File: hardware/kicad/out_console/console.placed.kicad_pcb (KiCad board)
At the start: 2 copper layers, 115 x 95 mm, 54 parts, among them J1 RaspberryPi_Pico_Common_THT, J10 JST_XH_B2B-XH-A_1x02_P2.50mm_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, J11 JST_XH_B2B-XH-A_1x02_P2.50mm_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, J12 JST_XH_B2B-XH-A_1x02_P2.50mm_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, J13 JST_XH_B2B-XH-A_1x02_P2.50mm_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, J14 JST_XH_B2B-XH-A_1x02_P2.50mm_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, J15 JST_XH_B2B-XH-A_1x02_P2.50mm_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, J16 JST_XH_B2B-XH-A_1x02_P2.50mm_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, J17 JST_XH_B2B-XH-A_1x02_P2.50mm_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, J18 JST_XH_B2B-XH-A_1x02_P2.50mm_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, J19 JST_XH_B2B-XH-A_1x02_P2.50mm_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, J2 IDC-Header_2x20_P2.54mm_Verti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, J20 JST_XH_B3B-XH-A_1x03_P2.50mm_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, J21 JST_XH_B3B-XH-A_1x03_P2.50mm_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, J22 PinHeader_2x04_P2.54mm_Vertic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, J3 JST_XH_B4B-XH-A_1x04_P2.50mm_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, J4 JST_XH_B3B-XH-A_1x03_P2.50mm_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, J5 JST_XH_B2B-XH-A_1x02_P2.50mm_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, J6 JST_XH_B8B-XH-A_1x08_P2.50mm_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, J7 JST_XH_B3B-XH-A_1x03_P2.50mm_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, J8 JST_XH_B2B-XH-A_1x02_P2.50mm_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, J9 JST_XH_B3B-XH-A_1x03_P2.50mm_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, U1 DIP-14_W7.62mm, U2 DIP-6_W7.62mm

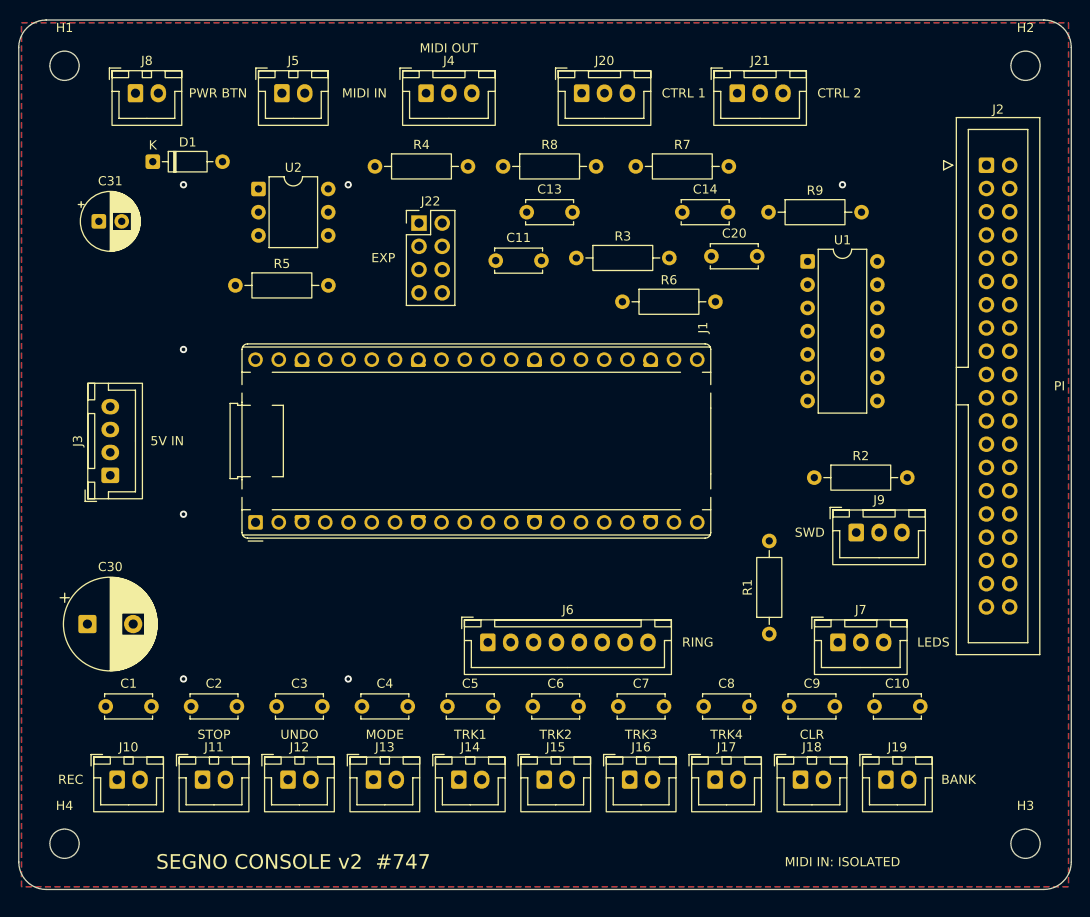
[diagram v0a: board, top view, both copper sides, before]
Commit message: style(hardware): put the console board's connectors and labels on shared lines
Purely cosmetic; no net or gate changes. The board read as scattered because
three separate things were each individually legal and collectively arbitrary:

- The rear-panel headers sat at 14/30/47/64/81 -- three different gaps, and the
  group off-centre. They are now on an even 17.5 mm pitch centred on x 54, the
  same centre line the switch row already used, and the resistors below them sit
  on those same centres rather than a 15 mm pitch of their own. Two pitches
  beating against each other is what made the band look crooked.
- Labels were placed by a nearest-free-gap search, so the rear-panel row came out
  "above, right, above, right, right" and REC sat left of its header while its
  nine neighbours sat above. The two rows that matter are now pinned to one y;
  the search remains as fallback for one-off headers.
- R1 was the only vertical resistor among twelve horizontals, which reads as an
  accident rather than a decision.

Still 0 DRC violations, 0 unconnected.

Refs #747
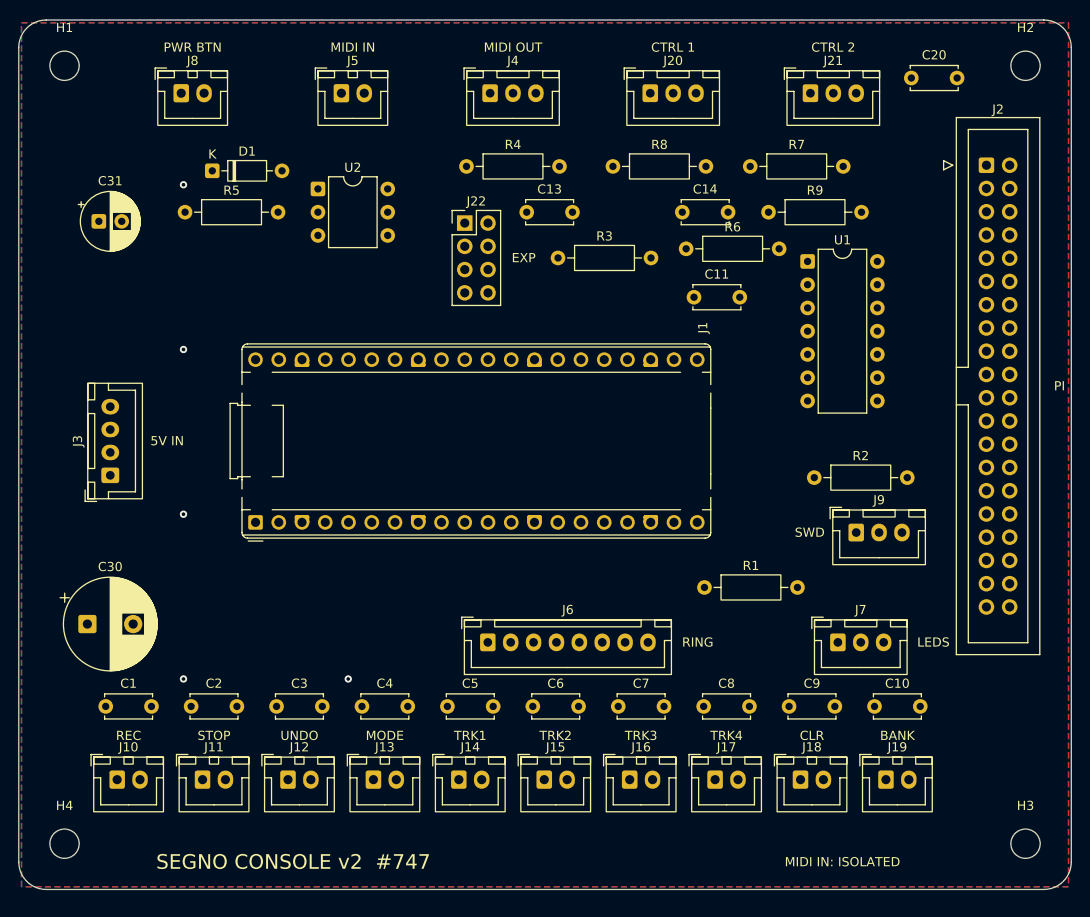
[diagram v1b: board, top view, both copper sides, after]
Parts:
- moved C20 29.3 mm to (197.5, 66.3)
- moved C11 22.0 mm to (173.8, 90.3)
- moved R7 12.5 mm to (179.9, 76.0)
- moved R8 12.0 mm to (164.9, 76.0)
- moved R4 10.0 mm to (148.9, 76.0)
- moved R5 9.71 mm to (118.2, 81.0)
- moved R6 9.05 mm to (172.9, 85.0)
- moved R1 8.71 mm to (174.9, 122.0), turned to 0 degrees
- moved J21 8.00 mm to (186.5, 68.0)
- moved J20 7.50 mm to (169.0, 68.0)
- moved J4 7.00 mm to (151.5, 68.0)
- moved D1 6.58 mm to (121.1, 76.5)
- moved J5 6.50 mm to (135.2, 68.0)
- moved U2 6.50 mm to (132.7, 78.5)
- moved J22 5.00 mm to (148.7, 82.2)
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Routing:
- net GND: vias 66 -> 64

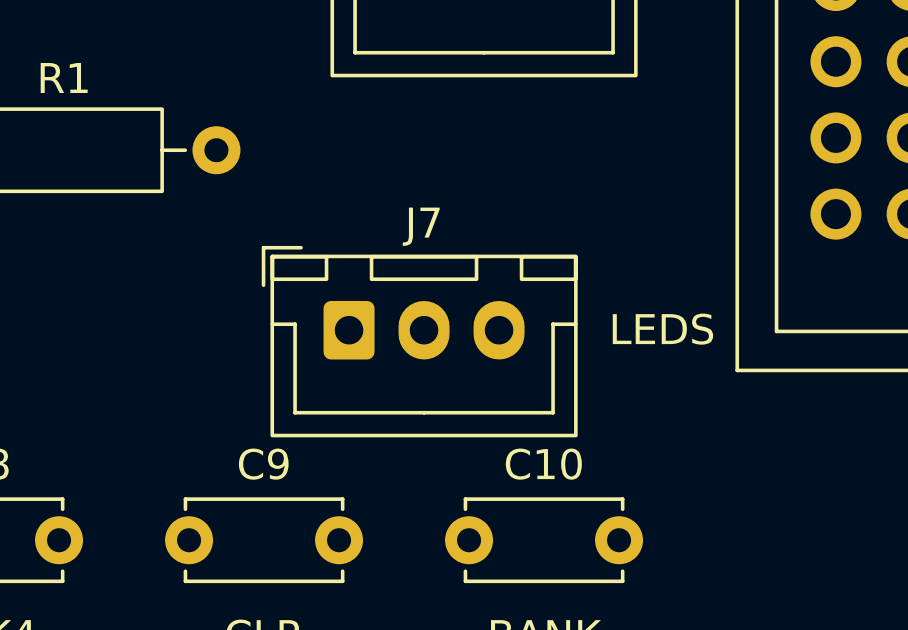
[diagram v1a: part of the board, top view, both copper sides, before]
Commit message: style(hardware): align J7 with J9 on the console board
Same 3-pin footprint, one directly below the other, sitting 2 mm apart in x --
which reads as a slip rather than a decision. No net changes; still 0 DRC
violations, 0 unconnected.

Refs #747
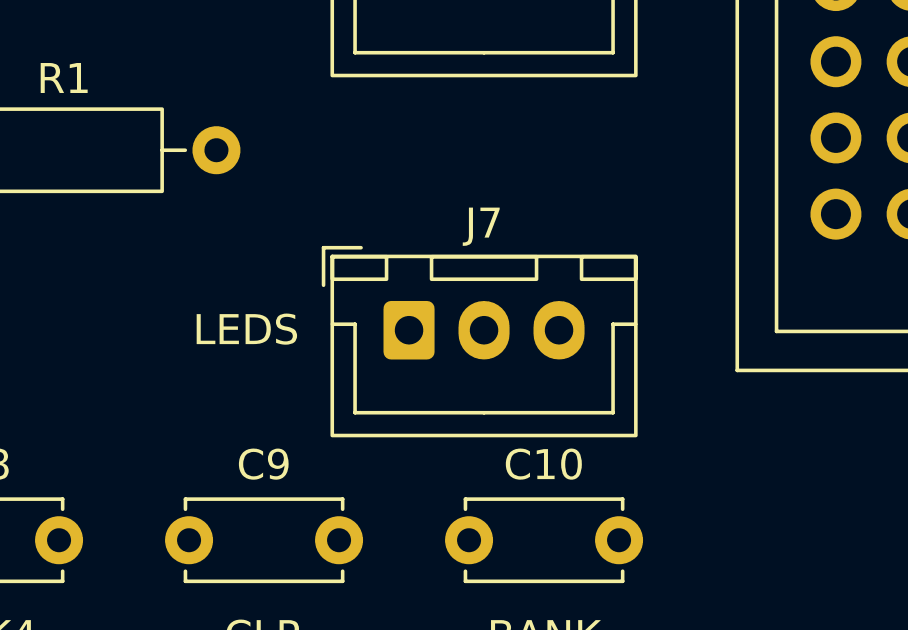
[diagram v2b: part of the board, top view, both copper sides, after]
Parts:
- moved J7 2.00 mm to (191.5, 128.0)

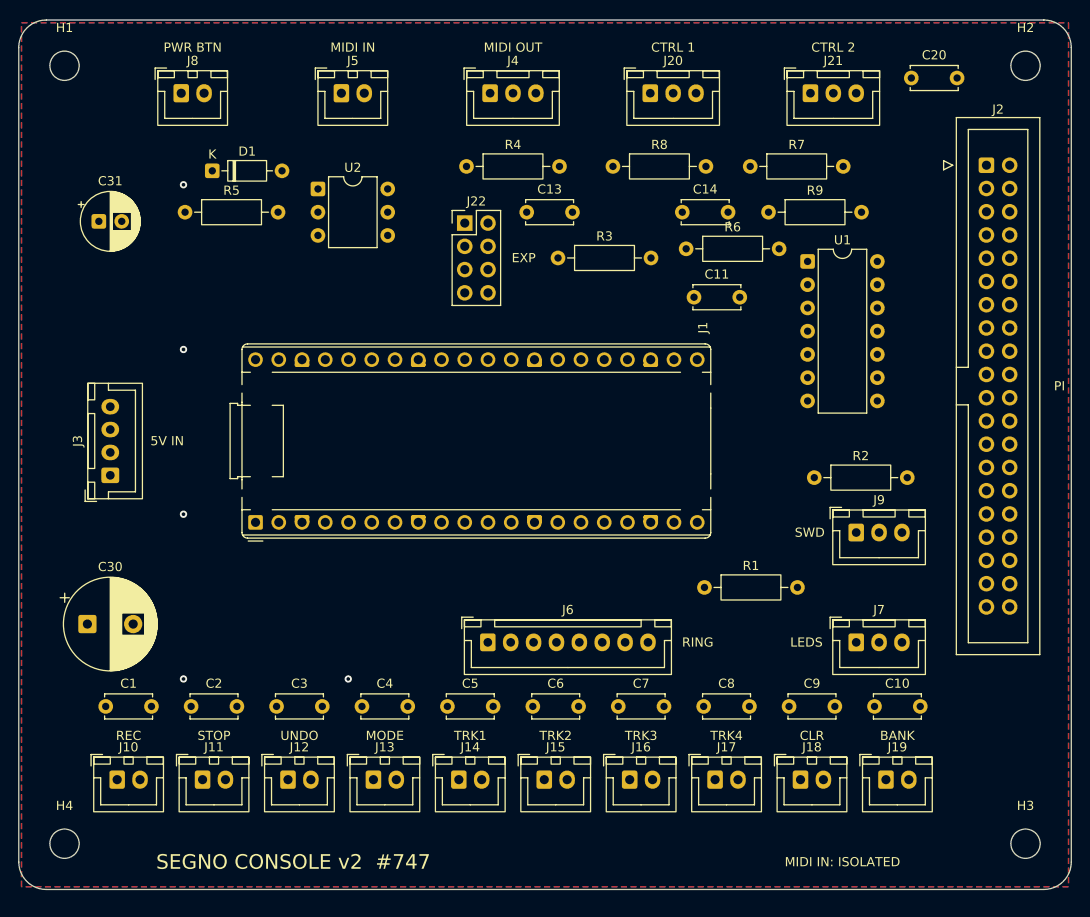
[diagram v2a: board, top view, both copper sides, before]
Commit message: feat(hardware): solder SWD to the Pico's own debug pads and centre the rows
The board would not route: RING_DATA had to climb from the module's row A to
U1's input through the corridor that the link, IND, EXP and CTRL nets all cross,
and J9 -- a 3-pin header breaking SWD out to flying wires -- sat in it. Centring
the pedal row made that corridor tighter still, so the two problems were one.

Both go away by dropping J9. Module:RaspberryPi_Pico_SMD_HandSolder carries the
three debug pads (D1/D2/D3) that the THT footprint does not, so SWCLK/GND/SWDIO
land straight on the module. The connector, its wires and the space it occupied
are gone. Conn_01x40 has no D pins, so they are added to the part explicitly --
otherwise SWD silently has nothing to attach to.

Trade: the module is soldered by its castellations, not socketed on headers, so
swapping one needs hot air. For a sealed console reflashed over SWD, correct.

Also: both connector rows now sit on the board's true centre (x 57.5) at an even
17.5 mm pitch -- the pedal row was 7.75 mm from the left edge and 14.75 from the
right -- and freerouting runs with -dct 0, cutting its 20 s idle timeout.

115x96 mm. 0 DRC violations, 0 unconnected, and it routes clean first attempt
rather than one roll in three.

Refs #747
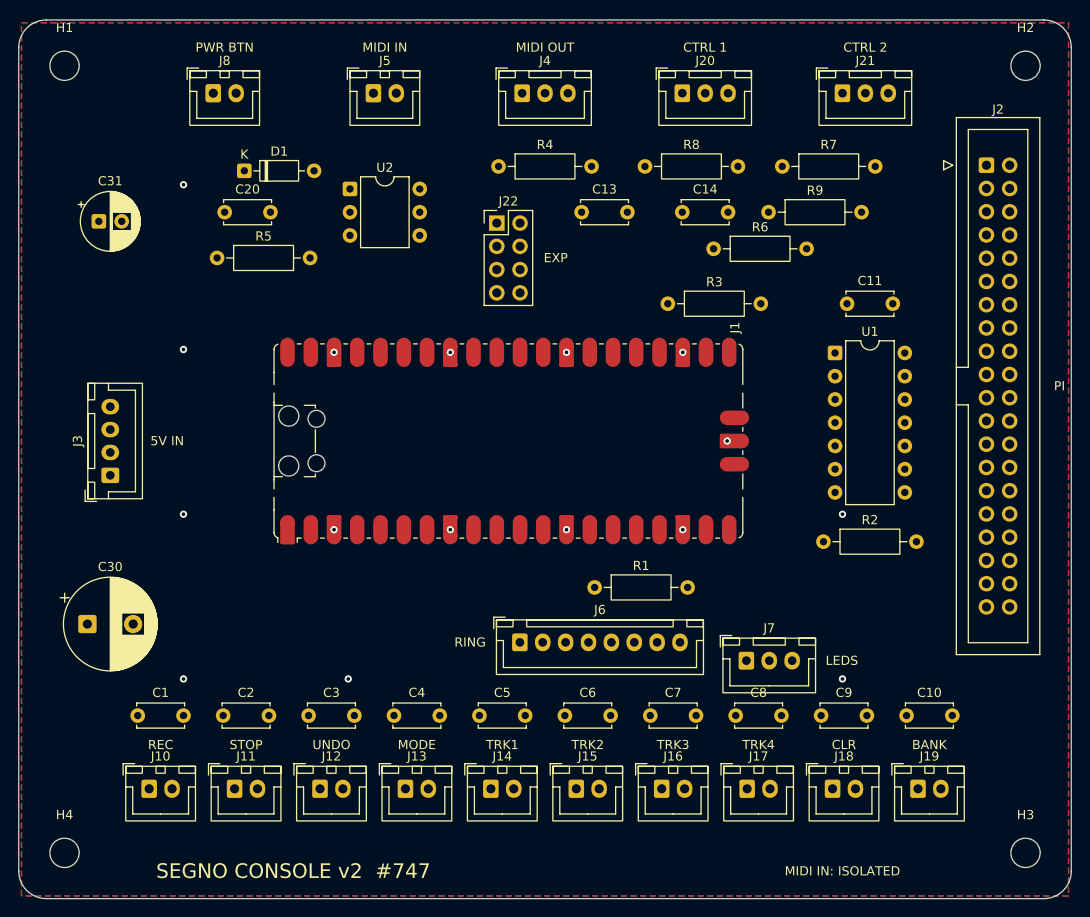
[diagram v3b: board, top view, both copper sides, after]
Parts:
- removed J9: JST_XH_B3B-XH-A_1x03_P2.50mm_Vertical, JST_XH_B3B-XH-A_1x03_P2.50mm_Vertical
- J1: value RaspberryPi_Pico_Common_THT -> RaspberryPi_Pico_SMD_HandSolder; footprint RaspberryPi_Pico_Common_THT -> RaspberryPi_Pico_SMD_HandSolder
- moved C20 76.4 mm to (122.5, 81.0)
- moved J1 29.0 mm to (153.5, 106.0)
- moved C11 16.7 mm to (190.5, 91.0)
- moved R3 13.0 mm to (170.9, 91.0)
- moved J7 12.2 mm to (179.5, 130.0)
- moved R1 12.0 mm to (162.9, 122.0)
- moved U1 10.4 mm to (189.2, 96.4)
- moved R2 7.07 mm to (187.9, 117.0)
- moved R5 6.10 mm to (121.7, 86.0)
- moved C13 6.00 mm to (161.5, 81.0)
- moved C1 3.64 mm to (113.0, 136.0)
- moved C10 3.64 mm to (197.0, 136.0)
- moved C2 3.64 mm to (122.3, 136.0)
- moved C3 3.64 mm to (131.7, 136.0)
- moved C4 3.64 mm to (141.0, 136.0)
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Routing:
- net GND: vias 64 -> 66
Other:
- board size 115 x 95 mm -> 115 x 96 mm
- board text removed: "SWD"

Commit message: fix(hardware): give the ground pours thermal relief now the Pico is SMD
The pours tied pads with solid copper. That was justified in a comment reading
"THT parts here are hand-soldered, so the usual thermal-relief argument
(wave/reflow) is moot" -- true when written, and false from the commit that made
the Pico a surface-mount module. Its nine GND pads sat in a plane on their own
layer with solid ties, which wicks the iron's heat into the plane and cold-joints
the one part that is painful to rework.

Solid was originally chosen to escape five "starved_thermal" errors from spokes
too narrow to form. That was a symptom of leaving the widths at their defaults,
not a reason to abandon relief: set explicitly (0.3 mm gap, 0.4 mm spokes) there
are none.

Two consequences, both real rather than cosmetic:
- Relief stops pads bridging the pour, which orphaned an F.Cu region. Stitch
  pitch drops 18 -> 12 mm (66 -> 83 vias). Relief and stitch pitch are one
  decision, not two.
- A 3 mm2 minimum island area drops slivers that reach a single pad and go
  nowhere; they cannot carry a return and they fail DRC as starved thermals.

Gated: any pour that ties pads solid while the board carries SMD pads now fails.
Nothing caught this transition, which is why it survived a footprint change.

0 DRC violations, 0 unconnected.

Refs #747
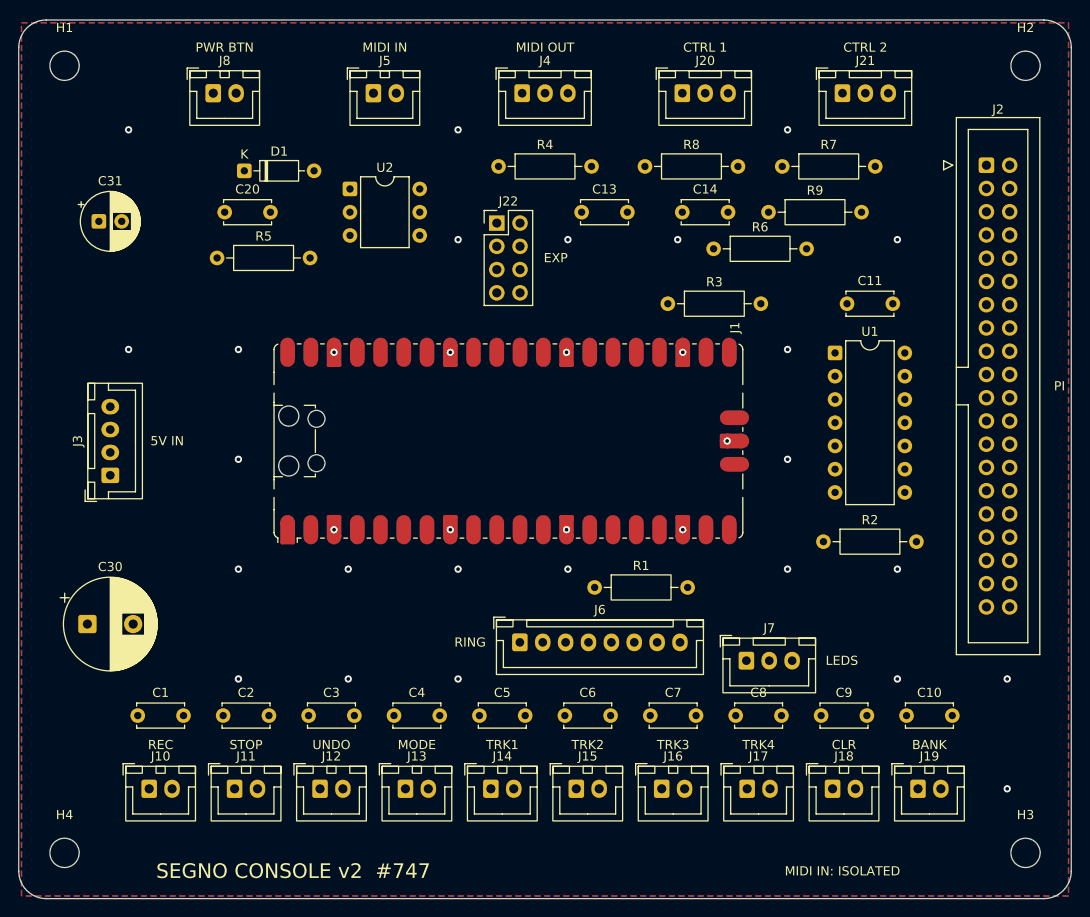
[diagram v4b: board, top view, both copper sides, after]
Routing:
- net GND: vias 66 -> 83

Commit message: fix(hardware): keep the module's USB corridor clear, and align J6 with J7
The 5 V inlet sat directly in front of the Pico's USB socket. The argument for
pointing that end into the bulk caps was that USB is not NEEDED -- VSYS is fed
from J3 and the Pi flashes over SWD -- but "not needed" quietly became "made
impossible", which is a different claim and not one anyone agreed to. J3 moves
down the left edge and C30 moves up, leaving y 40..52 clear from the socket to
the board edge.

Gated, with a negative control that reproduces exactly the shipped mistake:
anything intruding on the corridor off the module's USB end now fails.

Also J6 (RING) and J7 (LEDS) sat at y 68 and 70 -- same footprint family, side by
side, two millimetres apart for no reason. Both on 69.

0 DRC violations, 0 unconnected.

Refs #747
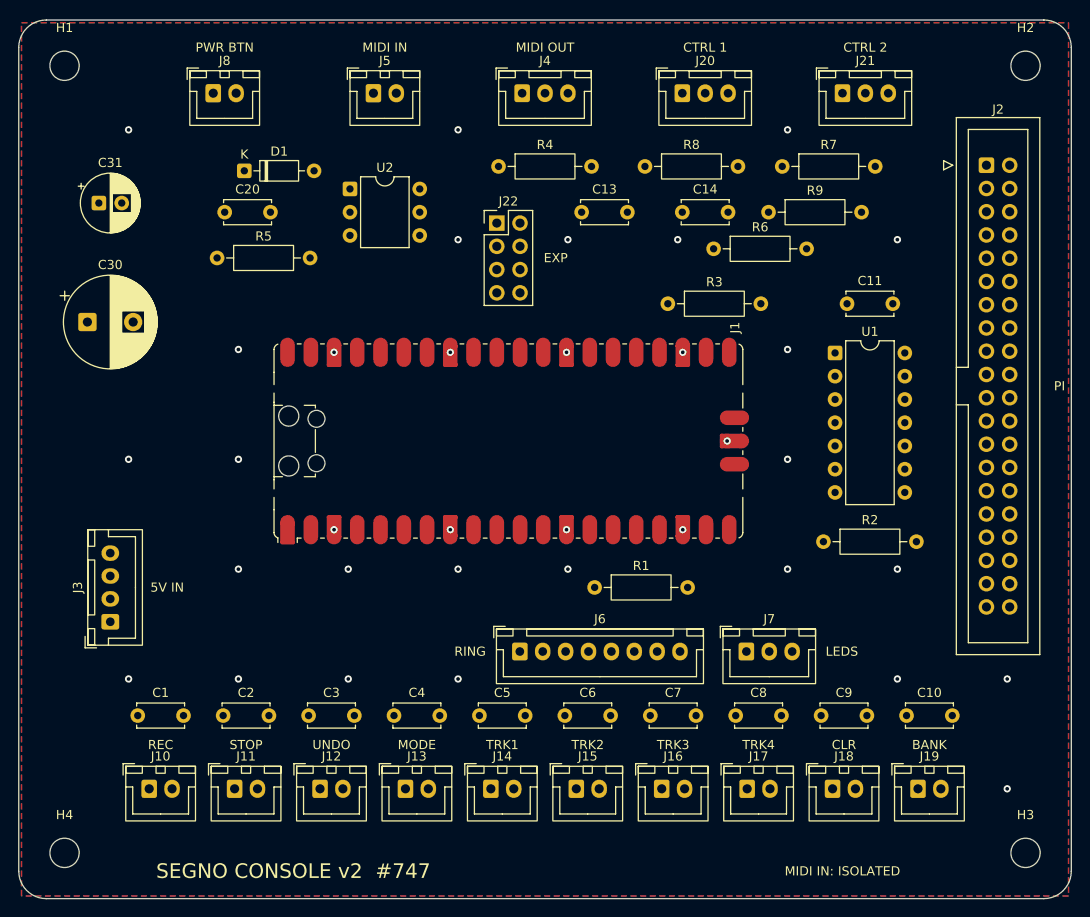
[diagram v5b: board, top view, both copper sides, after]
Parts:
- moved C30 33.0 mm to (107.5, 93.0)
- moved J3 16.0 mm to (110.0, 125.8)
- moved C31 2.00 mm to (108.8, 80.0)
- moved J6 1.00 mm to (154.8, 129.0)
- moved J7 1.00 mm to (179.5, 129.0)
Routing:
- net GND: vias 83 -> 84

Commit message: fix(hardware): merge the 5V rails; stop DRC hiding warnings
J3 becomes two parallel +5V/GND pairs instead of a +5V / +5V_LED split. Both
rails came off the same buck, so it was never redundancy or headroom, and the
IR-drop isolation it claimed was half undone by GND being a single pour. Doubling
the contacts buys the thing that is actually scarce: JST XH is ~3 A per contact.
The ring board is unaffected -- it names its own single supply +5V_LED locally,
and two netlists joined by a cable need only agree on pin order, which J6 keeps.

Separately, and worse: the DRC step ran --severity-error, so every '0 violations'
this pipeline has reported was errors-only. The board carries 131 warnings --
100 holes_co_located, 30 via_dangling, 1 starved_thermal. Now --severity-all.

Refs #747
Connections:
- C30 pad 1: +5V_LED -> +5V
- J3 pad 3: +5V_LED -> +5V
- J6 pad 1: +5V_LED -> +5V
- J6 pad 2: +5V_LED -> +5V
- J7 pad 1: +5V_LED -> +5V
